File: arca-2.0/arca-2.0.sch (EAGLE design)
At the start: 204 parts, among them IC1 MCP6N11R, IC2 MCP6N11R, IC3 MCP6N11R, IC4 MCP6N11R, IC5 LM324D, IC6 LM324D, SW1 1101M2S3CQE2, SW2 1101M2S3CQE2, T1 FQP30N06L, T2 FQP30N06L, T3 FQP30N06L, T4 FQP30N06L, T5 FQP30N06L, T6 FQP30N06L, X1 2540-5

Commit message: values tweaks as we make a BOM
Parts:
- DRV_STAT_1, DRV_STAT_2, DRV_STAT_3, DRV_STAT_4, DRV_STAT_5, DRV_STAT_6: value (none) -> YLW
- FS_STAT_1, FS_STAT_2, FS_STAT_3, FS_STAT_4, FS_STAT_5, FS_STAT_6, HBT: value (none) -> BLU
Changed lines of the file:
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@@
 <part name="GND11" library="supply1" library_urn="urn:adsk.eagle:library:371" deviceset="GND" device=""/>
 <part name="R8" library="rcl" library_urn="urn:adsk.eagle:library:334" deviceset="R-US_" device="R1206" package3d_urn="urn:adsk.eagle:package:23540/2" value="220"/>
-<part name="FS_STAT_1" library="led" library_urn="urn:adsk.eagle:library:259" deviceset="LED" device="CHIPLED_1206" package3d_urn="urn:adsk.eagle:package:15823/2"/>
+<part name="FS_STAT_1" library="led" library_urn="urn:adsk.eagle:library:259" deviceset="LED" device="CHIPLED_1206" package3d_urn="urn:adsk.eagle:package:15823/2" value="BLU"/>
 <part name="CON_DRV1" library="con-phoenix-5mm" deviceset="LPTA-2POS" device=""/>
 <part name="R9" library="rcl" library_urn="urn:adsk.eagle:library:334" deviceset="R-US_" device="R1206" package3d_urn="urn:adsk.eagle:package:23540/2" value="220"/>
-<part name="DRV_STAT_1" library="led" library_urn="urn:adsk.eagle:library:259" deviceset="LED" device="CHIPLED_1206" package3d_urn="urn:adsk.eagle:package:15823/2"/>
+<part name="DRV_STAT_1" library="led" library_urn="urn:adsk.eagle:library:259" deviceset="LED" device="CHIPLED_1206" package3d_urn="urn:adsk.eagle:package:15823/2" value="YLW"/>
 <part name="P+3" library="supply1" library_urn="urn:adsk.eagle:library:371" deviceset="+12V" device=""/>
 <part name="D5" library="diode-ss" deviceset="SS54" device=""/>
@@
 <part name="GND14" library="supply1" library_urn="urn:adsk.eagle:library:371" deviceset="GND" device=""/>
 <part name="R11" library="rcl" library_urn="urn:adsk.eagle:library:334" deviceset="R-US_" device="R1206" package3d_urn="urn:adsk.eagle:package:23540/2" value="220"/>
-<part name="FS_STAT_2" library="led" library_urn="urn:adsk.eagle:library:259" deviceset="LED" device="CHIPLED_1206" package3d_urn="urn:adsk.eagle:package:15823/2"/>
+<part name="FS_STAT_2" library="led" library_urn="urn:adsk.eagle:library:259" deviceset="LED" device="CHIPLED_1206" package3d_urn="urn:adsk.eagle:package:15823/2" value="BLU"/>
 <part name="CON_DRV2" library="con-phoenix-5mm" deviceset="LPTA-2POS" device=""/>
 <part name="R12" library="rcl" library_urn="urn:adsk.eagle:library:334" deviceset="R-US_" device="R1206" package3d_urn="urn:adsk.eagle:package:23540/2" value="220"/>
-<part name="DRV_STAT_2" library="led" library_urn="urn:adsk.eagle:library:259" deviceset="LED" device="CHIPLED_1206" package3d_urn="urn:adsk.eagle:package:15823/2"/>
+<part name="DRV_STAT_2" library="led" library_urn="urn:adsk.eagle:library:259" deviceset="LED" device="CHIPLED_1206" package3d_urn="urn:adsk.eagle:package:15823/2" value="YLW"/>
 <part name="P+4" library="supply1" library_urn="urn:adsk.eagle:library:371" deviceset="+12V" device=""/>
 <part name="D6" library="diode-ss" deviceset="SS54" device=""/>
@@
 <part name="GND17" library="supply1" library_urn="urn:adsk.eagle:library:371" deviceset="GND" device=""/>
 <part name="R14" library="rcl" library_urn="urn:adsk.eagle:library:334" deviceset="R-US_" device="R1206" package3d_urn="urn:adsk.eagle:package:23540/2" value="220"/>
-<part name="FS_STAT_3" library="led" library_urn="urn:adsk.eagle:library:259" deviceset="LED" device="CHIPLED_1206" package3d_urn="urn:adsk.eagle:package:15823/2"/>
+<part name="FS_STAT_3" library="led" library_urn="urn:adsk.eagle:library:259" deviceset="LED" device="CHIPLED_1206" package3d_urn="urn:adsk.eagle:package:15823/2" value="BLU"/>
 <part name="CON_DRV3" library="con-phoenix-5mm" deviceset="LPTA-2POS" device=""/>
 <part name="R15" library="rcl" library_urn="urn:adsk.eagle:library:334" deviceset="R-US_" device="R1206" package3d_urn="urn:adsk.eagle:package:23540/2" value="220"/>
-<part name="DRV_STAT_3" library="led" library_urn="urn:adsk.eagle:library:259" deviceset="LED" device="CHIPLED_1206" package3d_urn="urn:adsk.eagle:package:15823/2"/>
+<part name="DRV_STAT_3" library="led" library_urn="urn:adsk.eagle:library:259" deviceset="LED" device="CHIPLED_1206" package3d_urn="urn:adsk.eagle:package:15823/2" value="YLW"/>
 <part name="P+5" library="supply1" library_urn="urn:adsk.eagle:library:371" deviceset="+12V" device=""/>
 <part name="D7" library="diode-ss" deviceset="SS54" device=""/>
@@
 <part name="GND20" library="supply1" library_urn="urn:adsk.eagle:library:371" deviceset="GND" device=""/>
 <part name="R17" library="rcl" library_urn="urn:adsk.eagle:library:334" deviceset="R-US_" device="R1206" package3d_urn="urn:adsk.eagle:package:23540/2" value="220"/>
-<part name="FS_STAT_4" library="led" library_urn="urn:adsk.eagle:library:259" deviceset="LED" device="CHIPLED_1206" package3d_urn="urn:adsk.eagle:package:15823/2"/>
+<part name="FS_STAT_4" library="led" library_urn="urn:adsk.eagle:library:259" deviceset="LED" device="CHIPLED_1206" package3d_urn="urn:adsk.eagle:package:15823/2" value="BLU"/>
 <part name="CON_DRV4" library="con-phoenix-5mm" deviceset="LPTA-2POS" device=""/>
 <part name="R18" library="rcl" library_urn="urn:adsk.eagle:library:334" deviceset="R-US_" device="R1206" package3d_urn="urn:adsk.eagle:package:23540/2" value="220"/>
-<part name="DRV_STAT_4" library="led" library_urn="urn:adsk.eagle:library:259" deviceset="LED" device="CHIPLED_1206" package3d_urn="urn:adsk.eagle:package:15823/2"/>
+<part name="DRV_STAT_4" library="led" library_urn="urn:adsk.eagle:library:259" deviceset="LED" device="CHIPLED_1206" package3d_urn="urn:adsk.eagle:package:15823/2" value="YLW"/>
 <part name="P+6" library="supply1" library_urn="urn:adsk.eagle:library:371" deviceset="+12V" device=""/>
 <part name="D8" library="diode-ss" deviceset="SS54" device=""/>
@@
 <part name="GND23" library="supply1" library_urn="urn:adsk.eagle:library:371" deviceset="GND" device=""/>
 <part name="R20" library="rcl" library_urn="urn:adsk.eagle:library:334" deviceset="R-US_" device="R1206" package3d_urn="urn:adsk.eagle:package:23540/2" value="220"/>
-<part name="FS_STAT_5" library="led" library_urn="urn:adsk.eagle:library:259" deviceset="LED" device="CHIPLED_1206" package3d_urn="urn:adsk.eagle:package:15823/2"/>
+<part name="FS_STAT_5" library="led" library_urn="urn:adsk.eagle:library:259" deviceset="LED" device="CHIPLED_1206" package3d_urn="urn:adsk.eagle:package:15823/2" value="BLU"/>
 <part name="CON_DRV5" library="con-phoenix-5mm" deviceset="LPTA-2POS" device=""/>
 <part name="R21" library="rcl" library_urn="urn:adsk.eagle:library:334" deviceset="R-US_" device="R1206" package3d_urn="urn:adsk.eagle:package:23540/2" value="220"/>
-<part name="DRV_STAT_5" library="led" library_urn="urn:adsk.eagle:library:259" deviceset="LED" device="CHIPLED_1206" package3d_urn="urn:adsk.eagle:package:15823/2"/>
+<part name="DRV_STAT_5" library="led" library_urn="urn:adsk.eagle:library:259" deviceset="LED" device="CHIPLED_1206" package3d_urn="urn:adsk.eagle:package:15823/2" value="YLW"/>
 <part name="P+7" library="supply1" library_urn="urn:adsk.eagle:library:371" deviceset="+12V" device=""/>
 <part name="D9" library="diode-ss" deviceset="SS54" device=""/>
@@
 <part name="GND26" library="supply1" library_urn="urn:adsk.eagle:library:371" deviceset="GND" device=""/>
 <part name="R23" library="rcl" library_urn="urn:adsk.eagle:library:334" deviceset="R-US_" device="R1206" package3d_urn="urn:adsk.eagle:package:23540/2" value="220"/>
-<part name="FS_STAT_6" library="led" library_urn="urn:adsk.eagle:library:259" deviceset="LED" device="CHIPLED_1206" package3d_urn="urn:adsk.eagle:package:15823/2"/>
+<part name="FS_STAT_6" library="led" library_urn="urn:adsk.eagle:library:259" deviceset="LED" device="CHIPLED_1206" package3d_urn="urn:adsk.eagle:package:15823/2" value="BLU"/>
 <part name="CON_DRV6" library="con-phoenix-5mm" deviceset="LPTA-2POS" device=""/>
 <part name="R24" library="rcl" library_urn="urn:adsk.eagle:library:334" deviceset="R-US_" device="R1206" package3d_urn="urn:adsk.eagle:package:23540/2" value="220"/>
-<part name="DRV_STAT_6" library="led" library_urn="urn:adsk.eagle:library:259" deviceset="LED" device="CHIPLED_1206" package3d_urn="urn:adsk.eagle:package:15823/2"/>
+<part name="DRV_STAT_6" library="led" library_urn="urn:adsk.eagle:library:259" deviceset="LED" device="CHIPLED_1206" package3d_urn="urn:adsk.eagle:package:15823/2" value="YLW"/>
 <part name="P+8" library="supply1" library_urn="urn:adsk.eagle:library:371" deviceset="+12V" device=""/>
 <part name="D10" library="diode-ss" deviceset="SS54" device=""/>
@@
 <part name="P+33" library="supply1" library_urn="urn:adsk.eagle:library:371" deviceset="+5V" device=""/>
 <part name="P+34" library="supply1" library_urn="urn:adsk.eagle:library:371" deviceset="+5V" device=""/>
-<part name="HBT" library="led" library_urn="urn:adsk.eagle:library:259" deviceset="LED" device="CHIPLED_1206" package3d_urn="urn:adsk.eagle:package:15823/2"/>
+<part name="HBT" library="led" library_urn="urn:adsk.eagle:library:259" deviceset="LED" device="CHIPLED_1206" package3d_urn="urn:adsk.eagle:package:15823/2" value="BLU"/>
 <part name="R77" library="rcl" library_urn="urn:adsk.eagle:library:334" deviceset="R-US_" device="R1206" package3d_urn="urn:adsk.eagle:package:23540/2" value="68"/>
 <part name="GND69" library="supply1" library_urn="urn:adsk.eagle:library:371" deviceset="GND" device=""/>

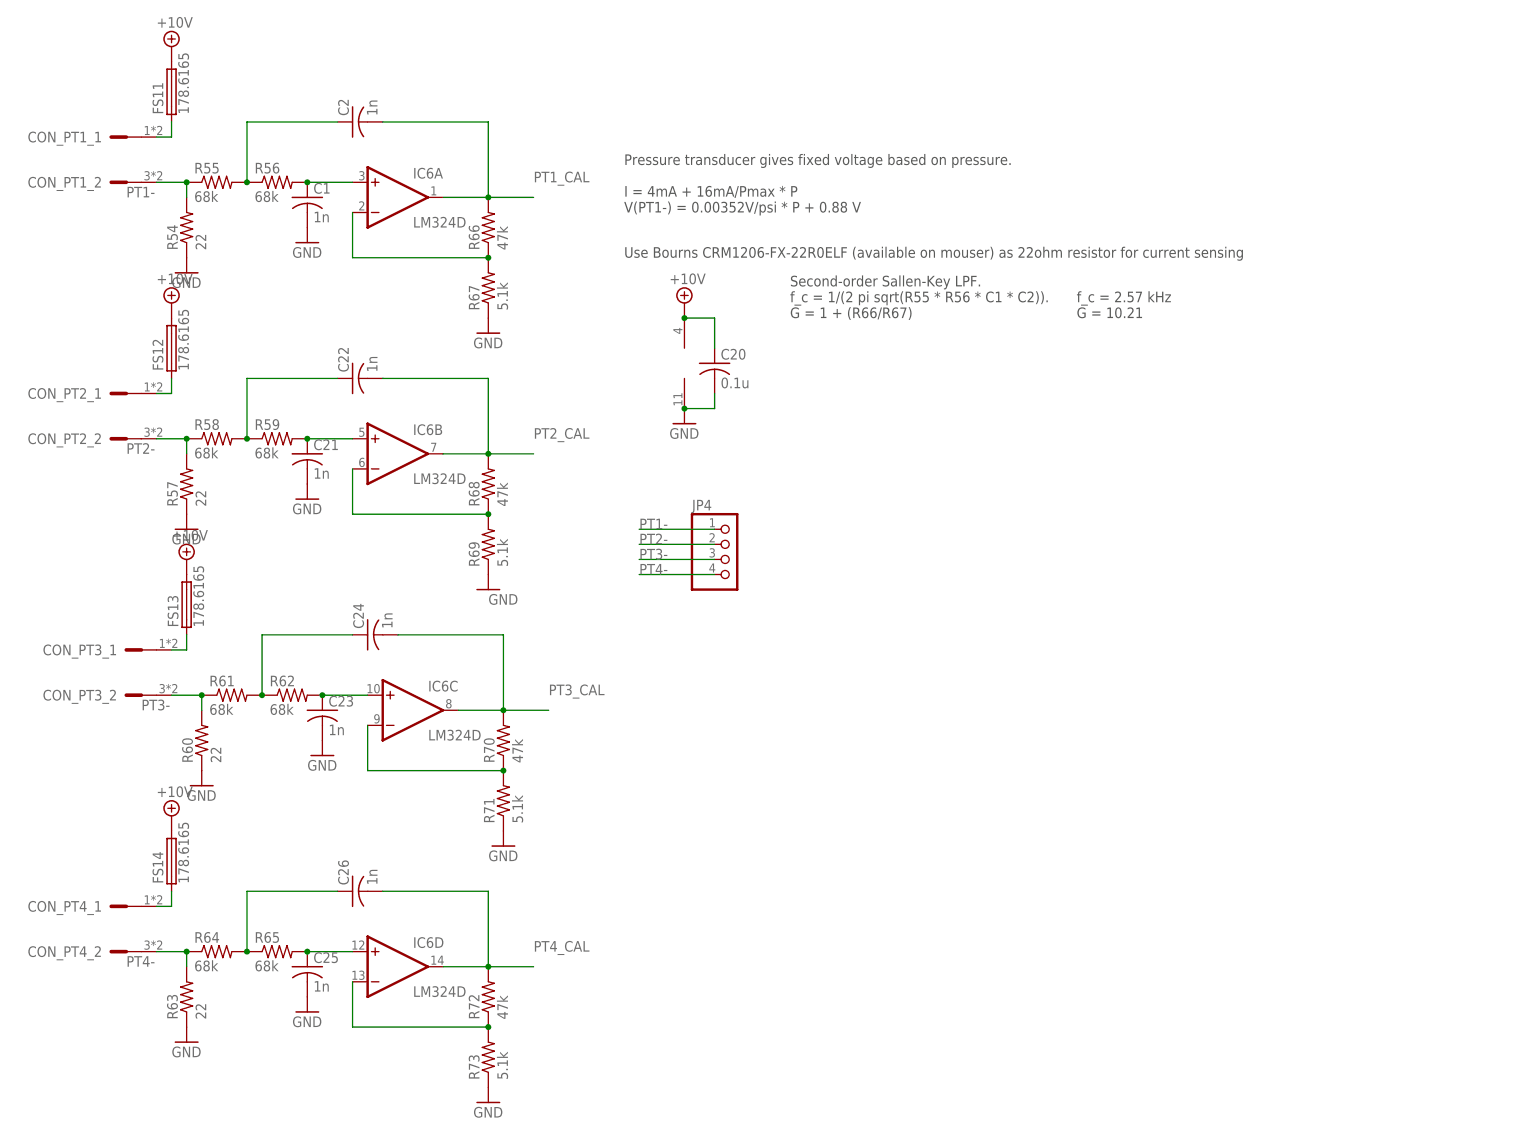
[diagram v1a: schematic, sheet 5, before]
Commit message: slight reshaping of schematic to make more human-readable
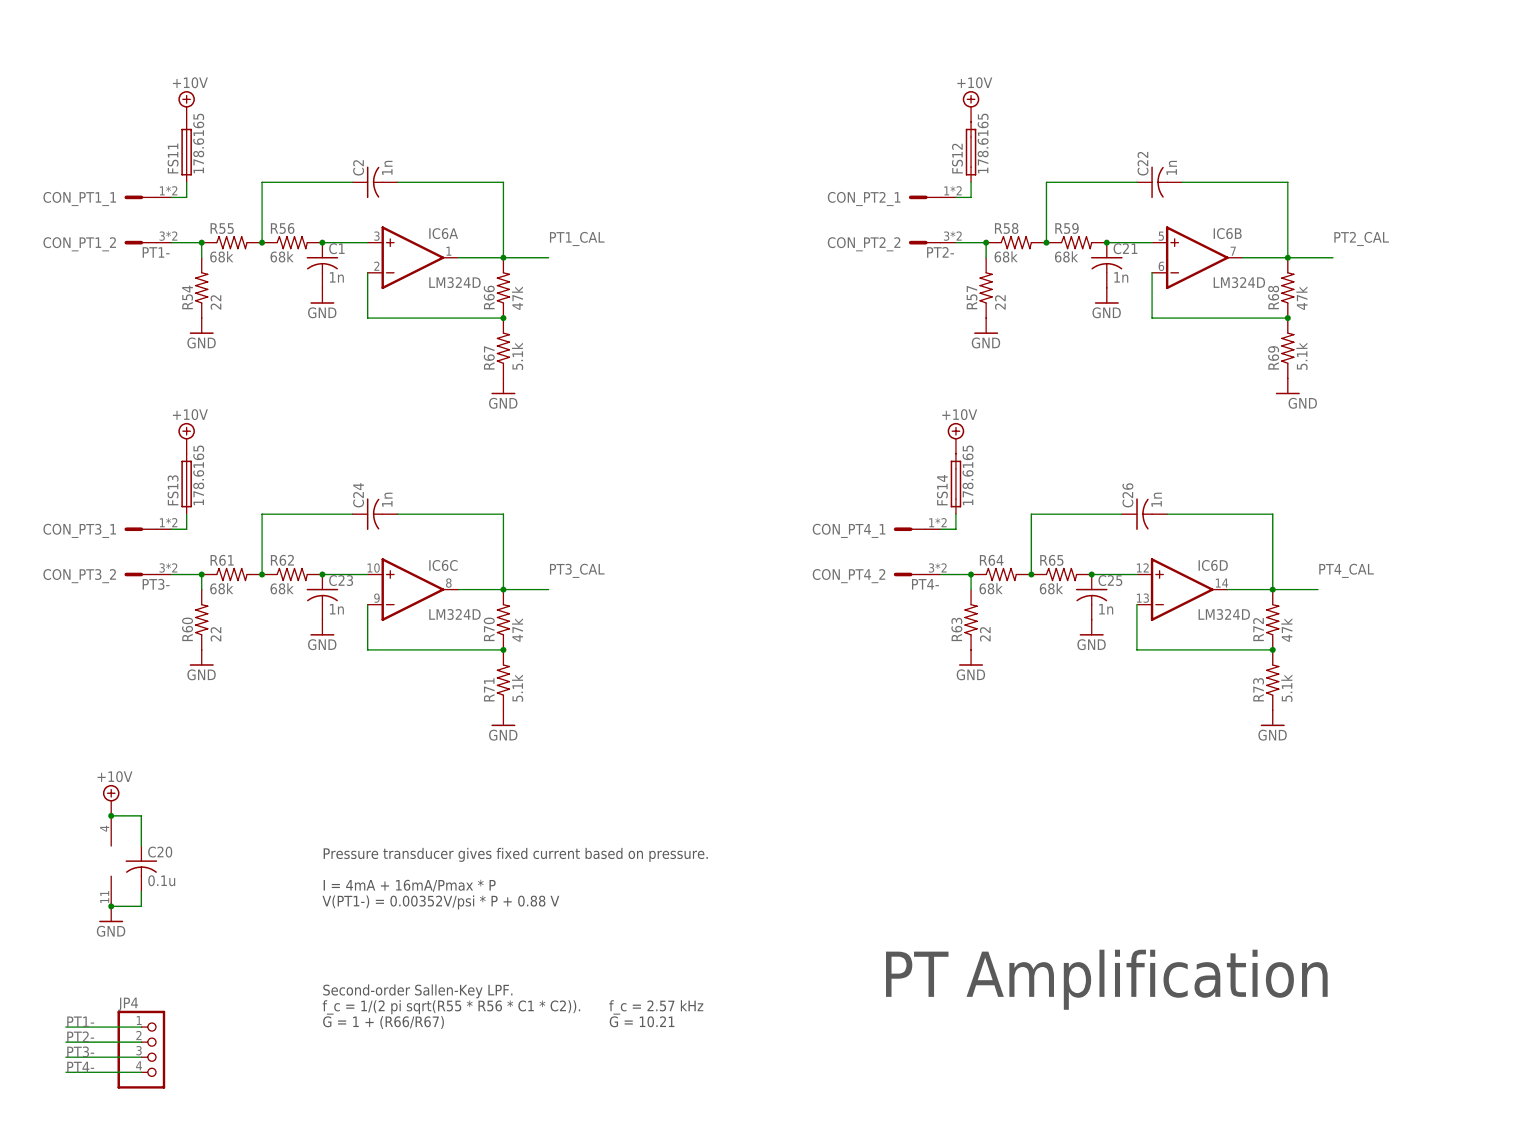
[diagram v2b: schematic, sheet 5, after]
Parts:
- C27, C28, C29: value 0.1u -> 100n
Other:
- note added: "ADCs"
- note added: "Drivers"
- note added: "G = RF1 / RG1 + 1 ~ 100x"
- note added: "LC Anti-Aliasing"
- note added: "Load Cell Inamps"
- note added: "PT Amplification"
- note added: "Pressure transducer gives fixed current based on pressure. I = 4mA + 16mA/Pmax * P V(PT1-) = 0.00352V/psi * P + 0.88 V"
- note added: "Raspberry Pi"
- note added: "Thermocouples"
- note removed: "Pressure transducer gives fixed voltage based on pressure. I = 4mA + 16mA/Pmax * P V(PT1-) = 0.00352V/psi * P + 0.88 V"
- note removed: "Use Bourns CRM1206-FX-22R0ELF (available on mouser) as 22ohm resistor for current sensing"
- moved on the sheet: C1, C2, C20, C21, C22, C23, C24, C25, C26, CON_PT1_1, CON_PT1_2, CON_PT2_1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
